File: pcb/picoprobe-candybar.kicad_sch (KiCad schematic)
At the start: 48 parts, among them J0 SWD-UART_PicoprobeCandybar, J1 PinHeader_2x04, J2 PinSocket_1x03, J3 PinSocket_1x02, J4 PinSocket_1x03, J5 PinSocket_1x03, J6 PinSocket_1x03, J7 PinSocket_1x02, Q1 T2N7002AK, Q2 DMP31D1U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

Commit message: Reorganize & label bottom-right schematic
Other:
- note added: "Analogue references"
- note added: "DAP conn. LED"
- note added: "DAP run LED"
- note added: "UART RX LED"
- note added: "UART TX LED"
- note removed: "Analogue ground"
- moved on the sheet: D1, D2, D3, D4, D5, R15, R16, R17, R18, SW2, SW3

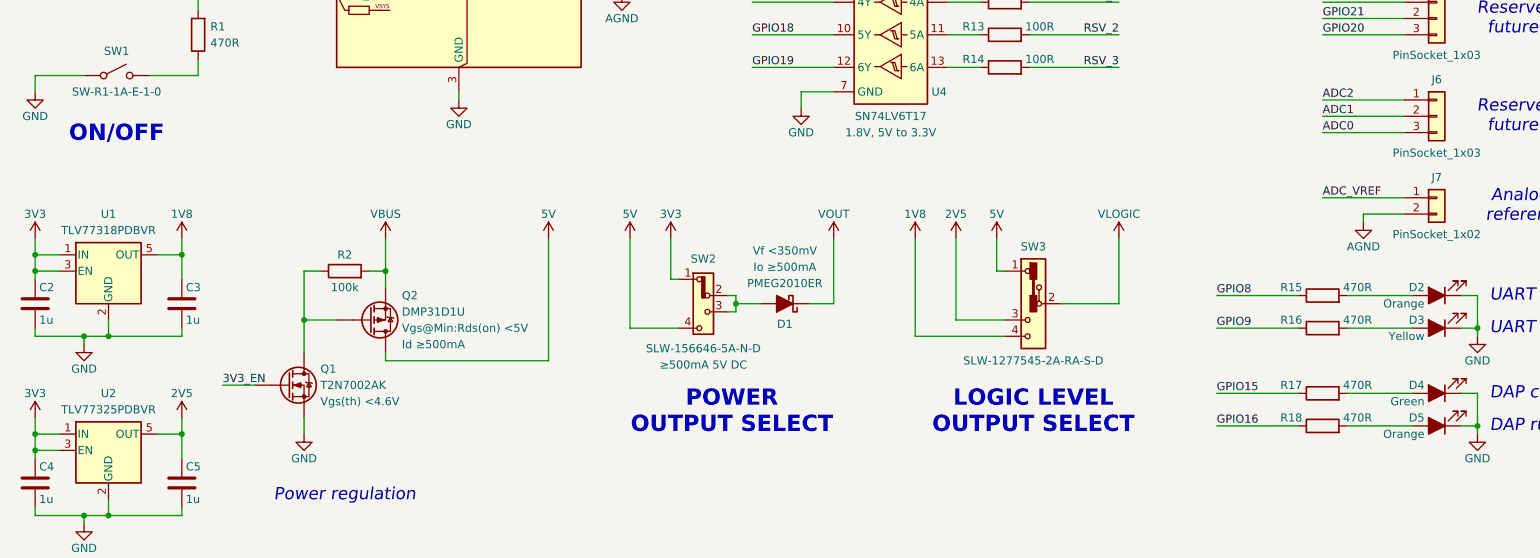
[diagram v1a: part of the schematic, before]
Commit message: Revise LED colours
Green: Connected
Red: Controlling/Halted
Orange: Transmitting
Yellow: Receiving
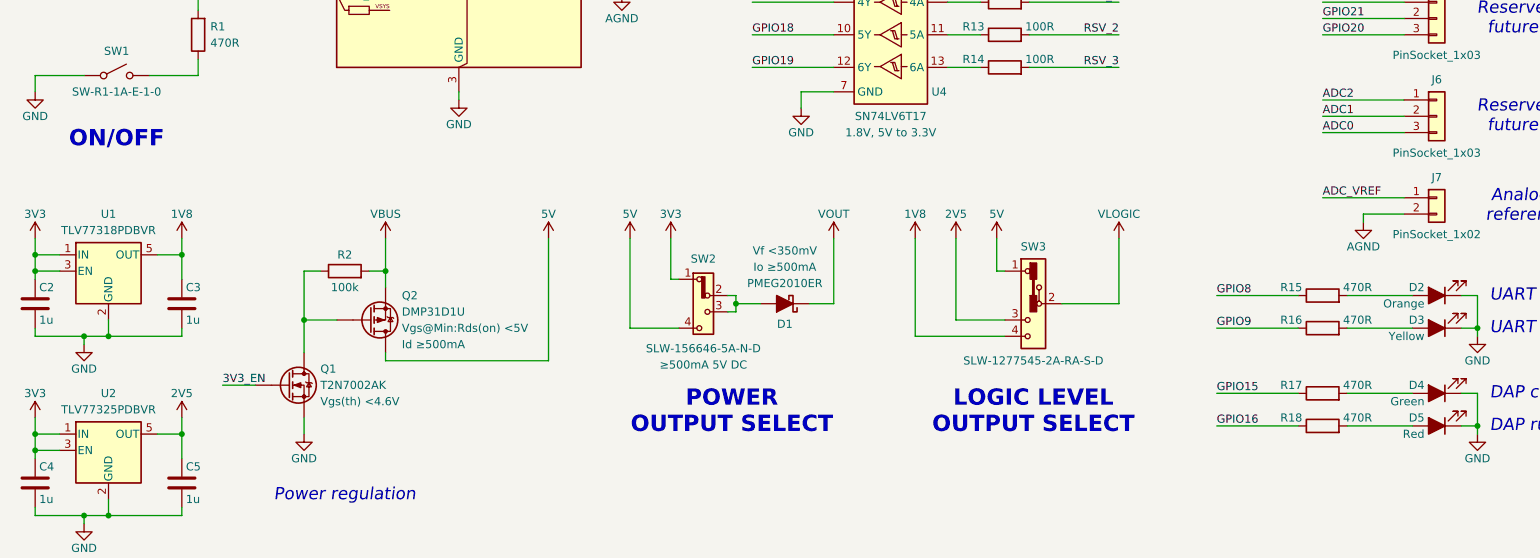
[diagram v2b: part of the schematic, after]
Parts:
- D5: value Orange -> Red
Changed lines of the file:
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@@
 	(text "ON/OFF"
 		(exclude_from_sim no)
-		(at 40.64 118.11 0)
+		(at 40.64 121.92 0)
 		(effects
 			(font
@@
 				(bold yes)
 			)
-			(justify top)
+			(justify bottom)
 		)
 	)
@@
 			)
 		)
-		(property "Value" "Orange"
+		(property "Value" "Red"
 			(at 244.475 166.37 0)
 			(effects

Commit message: Add mounting holes
Also switches Pico footprint to have mounting holes
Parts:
- A1: footprint Module_RaspberryPi_Pico:RaspberryPi_Pico_Original_SMD_HandSolder -> Module_RaspberryPi_Pico:RaspberryPi_Pico_Original_SMD_MountingHoles_HandSolder
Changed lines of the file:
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@@
 			)
 		)
-		(property "Footprint" "Module_RaspberryPi_Pico:RaspberryPi_Pico_Original_SMD_HandSolder"
+		(property "Footprint" "Module_RaspberryPi_Pico:RaspberryPi_Pico_Original_SMD_MountingHoles_HandSolder"
 			(at 93.98 124.46 0)
 			(effects

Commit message: Consolidate C2/C4 & reorganize schematic
Also changes sockets to placeholder SMD footprints
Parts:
- removed C4: 1u, Capacitor_SMD:C_0805_2012Metric_Pad1.18x1.45mm_HandSolder, symbol Device:C
- J2: footprint Connector_PinSocket_2.54mm:PinSocket_1x03_P2.54mm_Horizontal -> Connector_PinSocket_2.54mm:PinSocket_1x02_P2.54mm_Vertical_SMD_Pin1Left
- J3, J7: footprint Connector_PinSocket_2.54mm:PinSocket_1x02_P2.54mm_Horizontal -> Connector_PinSocket_2.54mm:PinSocket_1x02_P2.54mm_Vertical_SMD_Pin1Left
- J4, J5, J6: footprint Connector_PinSocket_2.54mm:PinSocket_1x03_P2.54mm_Horizontal -> Connector_PinSocket_2.54mm:PinSocket_1x03_P2.54mm_Vertical_SMD_Pin1Left
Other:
- moved on the sheet: C2, C3, C5, D1, Q1, Q2, R2, SW2, SW3, U1, U2

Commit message: Add filtering cap to VOUT
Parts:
- added C4: 1u, Capacitor_SMD:C_0805_2012Metric_Pad1.18x1.45mm_HandSolder, symbol Device:C
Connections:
- net GND: now also C4.2
- net VOUT: now also C4.1
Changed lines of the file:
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@@
 	)
 	(junction
+		(at 222.25 43.18)
+		(diameter 0)
+		(color 0 0 0 0)
+	)
+	(junction
 		(at 43.18 157.48)
 		(diameter 0)
@@
 	(wire
 		(pts
-			(xy 252.73 43.18) (xy 270.51 43.18)
-		)
-		(stroke
-			(width 0)
-			(type default)
-		)
-	)
-	(wire
-		(pts
 			(xy 34.29 64.77) (xy 34.29 66.04)
 		)
@@
 	(wire
 		(pts
+			(xy 222.25 40.64) (xy 222.25 43.18)
+		)
+		(stroke
+			(width 0)
+			(type default)
+		)
+	)
+	(wire
+		(pts
 			(xy 232.41 165.1) (xy 242.57 165.1)
 		)
@@
 	(wire
 		(pts
+			(xy 270.51 43.18) (xy 252.73 43.18)
+		)
+		(stroke
+			(width 0)
+			(type default)
+		)
+	)
+	(wire
+		(pts
 			(xy 45.72 110.49) (xy 53.34 110.49)
 		)
@@
 	(wire
 		(pts
+			(xy 222.25 30.48) (xy 222.25 33.02)
+		)
+		(stroke
+			(width 0)
+			(type default)
+		)
+	)
+	(wire
+		(pts
 			(xy 252.73 38.1) (xy 264.16 38.1)
 		)
@@
 	)
 	(symbol
+		(lib_id "Device:C")
+		(at 222.25 36.83 0)
+		(unit 1)
+		(exclude_from_sim no)
+		(in_bom yes)
+		(on_board yes)
+		(dnp no)
+		(property "Reference" "C4"
+			(at 222.885 34.29 0)
+			(effects
+				(font
+					(size 1.27 1.27)
+				)
+				(justify left)
+			)
+		)
+		(property "Value" "1u"
+			(at 222.885 39.37 0)
+			(effects
+				(font
+					(size 1.27 1.27)
+				)
+				(justify left)
+			)
+		)
+		(property "Footprint" "Capacitor_SMD:C_0805_2012Metric_Pad1.18x1.45mm_HandSolder"
+			(at 223.2152 40.64 0)
+			(effects
+				(font
+					(size 1.27 1.27)
+				)
+				(hide yes)
+			)
+		)
+		(property "Datasheet" "~"
+			(at 222.25 36.83 0)
+			(effects
+				(font
+					(size 1.27 1.27)
+				)
+				(hide yes)
+			)
+		)
+		(property "Description" "Unpolarized capacitor"
+			(at 222.25 36.83 0)
+			(effects
+				(font
+					(size 1.27 1.27)
+				)
+				(hide yes)
+			)
+		)
+		(pin "1"
+		)
+		(pin "2"
+		)
+		(instances
+			(project "picoprobe-candybar"
+				(path "/73798b73-b835-4423-abd2-5bd613a215bf"
+					(reference "C4")
+					(unit 1)
+				)
+			)
+		)
+	)
+	(symbol
 		(lib_id "power:VCC")
 		(at 34.29 30.48 0)
@@
 					(unit 1)
 				)
+			)
+		)
+	)
+	(symbol
+		(lib_id "power:VCC")
+		(at 222.25 30.48 0)
+		(unit 1)
+		(exclude_from_sim no)
+		(in_bom yes)
+		(on_board yes)
+		(dnp no)
+		(property "Reference" "#PWR038"
+			(at 222.25 34.29 0)
+			(effects
+				(font
+					(size 1.27 1.27)
+				)
+				(hide yes)
+			)
+		)
+		(property "Value" "VOUT"
+			(at 222.25 26.67 0)
+			(effects
+				(font
+					(size 1.27 1.27)
+				)
+			)
+		)
+		(property "Footprint" ""
+			(at 222.25 30.48 0)
+			(effects
+				(font
+					(size 1.27 1.27)
+				)
+				(hide yes)
+			)
+		)
+		(property "Datasheet" ""
+			(at 222.25 30.48 0)
+			(effects
+				(font
+					(size 1.27 1.27)
+				)
+				(hide yes)
+			)
+		)
+		(property "Description" "Power symbol creates a global label with name \"VOUT\""
+			(at 222.25 30.48 0)
+			(effects
+				(font
+					(size 1.27 1.27)
+				)
+				(hide yes)
+			)
+		)
+		(pin "1"
+		)
+		(instances
+			(project "picoprobe-candybar"
+				(path "/73798b73-b835-4423-abd2-5bd613a215bf"
+					(reference "#PWR038")
+					(unit 1)
+				)

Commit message: Don't level-shift nRESET output signal
Needs to behave as an open drain
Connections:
- net CB_~{RST}: now also A1.4 (GPIO2)
- net GPIO2: now also R6.1; no longer A1.4 (GPIO2), U3.9 (4A)
- net at U3.8 (4Y): no longer R6.1
- no-connect marks 2 -> 4
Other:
- moved on the sheet: C6, C7, R10, R11, R12, R13, R14, R3, R4, R5, R6, R7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

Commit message: Swap 100R and 470R resistors for resistor arrays
More compact board layout, and more cost-effective
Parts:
- removed R10, R11, R12, R13, R14, R3, R4, R5, R6, R7, R8, R9: 100R, Resistor_SMD:R_0805_2012Metric_Pad1.20x1.40mm_HandSolder, symbol Device:R
- removed R15, R16, R17, R18: 470R, Resistor_SMD:R_0805_2012Metric_Pad1.20x1.40mm_HandSolder, symbol Device:R
- added RN1, RN2, RN4: 100R, Resistor_SMD:R_Array_Convex_4x1206, symbol Device:R_Pack04_Split
- added RN3: 470R, Resistor_SMD:R_Array_Convex_4x1206, symbol Device:R_Pack04_Split
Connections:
- net CB_CLK: now also RN2.8 (R1.2)
- net CB_CTS: now also RN2.5 (R4.2)
- net CB_DTR: now also RN1.8 (R1.2)
- net CB_IO: now also RN2.7 (R2.2), RN4.8 (R1.2)
- net CB_RTS: now also RN1.6 (R3.2)
- net CB_RX: now also RN2.6 (R3.2)
- net CB_TX: now also RN1.7 (R2.2)
- net CB_~{RST}: now also RN1.5 (R4.2)
- net GPIO15: now also RN3.3 (R3.1)
- net GPIO16: now also RN3.4 (R4.1)
- net GPIO2: now also RN1.4 (R4.1)
- net GPIO8: now also RN3.1 (R1.1)
- net GPIO9: now also RN3.2 (R2.1)
- net RSV_1: now also RN4.7 (R2.2)
- net RSV_2: now also RN4.6 (R3.2)
- net RSV_3: now also RN4.5 (R4.2)
- net at U4.3 (2A): now also RN2.4 (R4.1)
- net at D4.2 (A): now also RN3.6 (R3.2)
- net at U3.10 (5Y): now also RN2.1 (R1.1)
- net at U3.12 (6Y): now also RN2.2 (R2.1)
- net at U3.2 (1Y): now also RN1.1 (R1.1)
- net at U3.4 (2Y): now also RN1.2 (R2.1)
- net at U3.6 (3Y): now also RN1.3 (R3.1)
- net at D5.2 (A): now also RN3.5 (R4.2)
- net at D2.2 (A): now also RN3.8 (R1.2)
- net at U4.5 (3A): now also RN4.1 (R1.1)
- net at D3.2 (A): now also RN3.7 (R2.2)
- net at U4.1 (1A): now also RN2.3 (R3.1)
- net at U4.11 (5A): now also RN4.3 (R3.1)
- net at U4.13 (6A): now also RN4.4 (R4.1)
- net at U4.9 (4A): now also RN4.2 (R2.1)
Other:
- moved on the sheet: C2, C3, C5, C6, C7, D1, Q2, R2, SW2, SW3, U1, U2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

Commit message: Move 100R from `CB_RST` to On/Off switch
`CB_RST` signal, if used, is not high-frequency, and thus does not need
a termination resistor.

On/Off switch series resistor simply needs to be below ~8k due to
voltage division (see commit `b02ed6a` for details)

RC charge ("Off") speed does not matter, and switch series resistor
value does not change the >20ms RC discharge ("On") speed
(see commit `1dfc5cb` for some additional details)

Using this resistor from an array saves us from a stray solo resistor.
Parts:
- removed R1: 470R, Resistor_SMD:R_0805_2012Metric_Pad1.20x1.40mm_HandSolder, symbol Device:R
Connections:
- net 3V3_EN: now also RN1.8 (R1.2)
- net CB_DTR: now also RN1.7 (R2.2); no longer RN1.8 (R1.2)
- net CB_RTS: now also RN1.5 (R4.2); no longer RN1.6 (R3.2)
- net CB_TX: now also RN1.6 (R3.2); no longer RN1.7 (R2.2)
- net CB_~{RST}: no longer RN1.5 (R4.2)
- net at SW1.2 (B): now also RN1.1 (R1.1)
- net at RN1.2 (R2.1): now also U3.2 (1Y); no longer U3.4 (2Y)
- net at RN1.3 (R3.1): now also U3.4 (2Y); no longer U3.6 (3Y)
- net GPIO2: no longer names the net of RN1.4 (R4.1)
- net GPIO2: now also U3.6 (3Y)
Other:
- moved on the sheet: C6, C7, RN1D, RN2A, RN2B, RN2C, RN2D, RN3A, RN3B, RN3C, RN3D, RN4A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
